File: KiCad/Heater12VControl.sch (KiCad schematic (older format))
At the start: 11 parts, among them J1 12V, J2 Arduino, J3 Heater, J4 Temp sensor, Q1 SI2308, Q2 IRLR3715

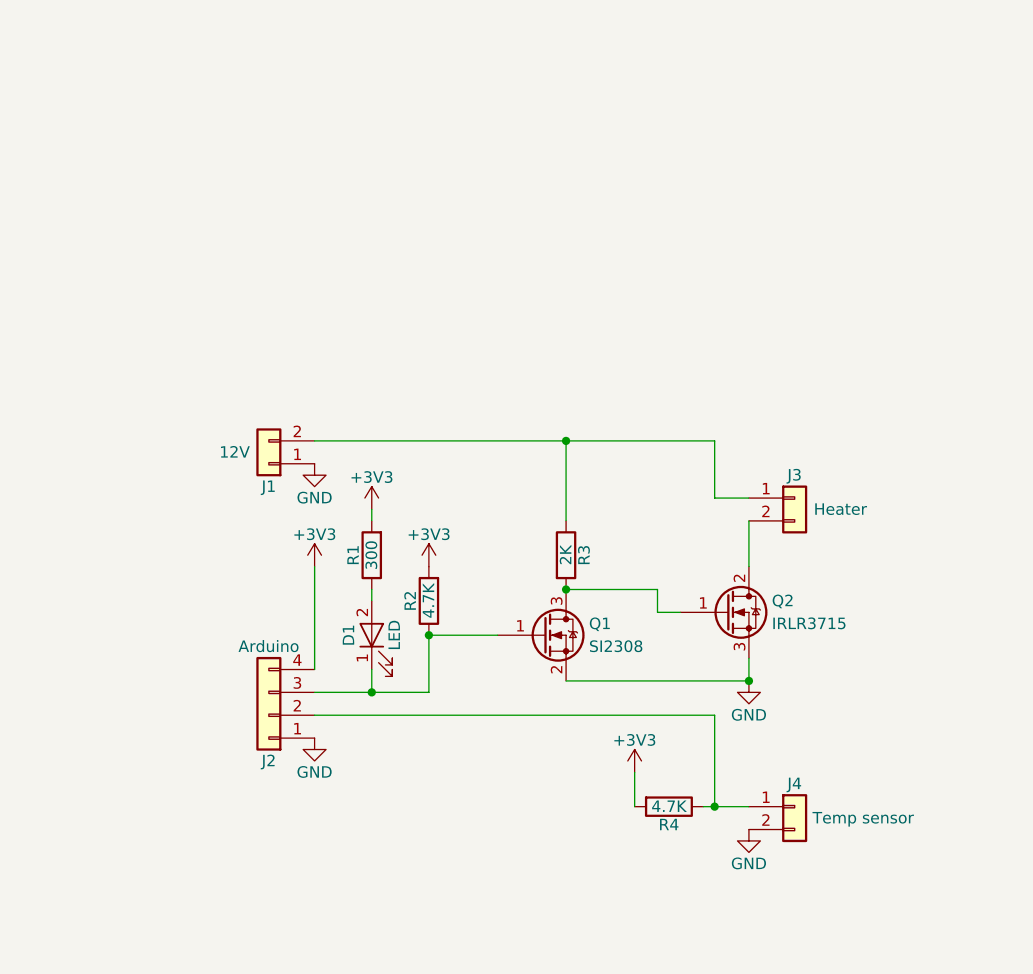
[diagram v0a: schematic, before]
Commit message: New Version with rotary encoder and AIO pcb
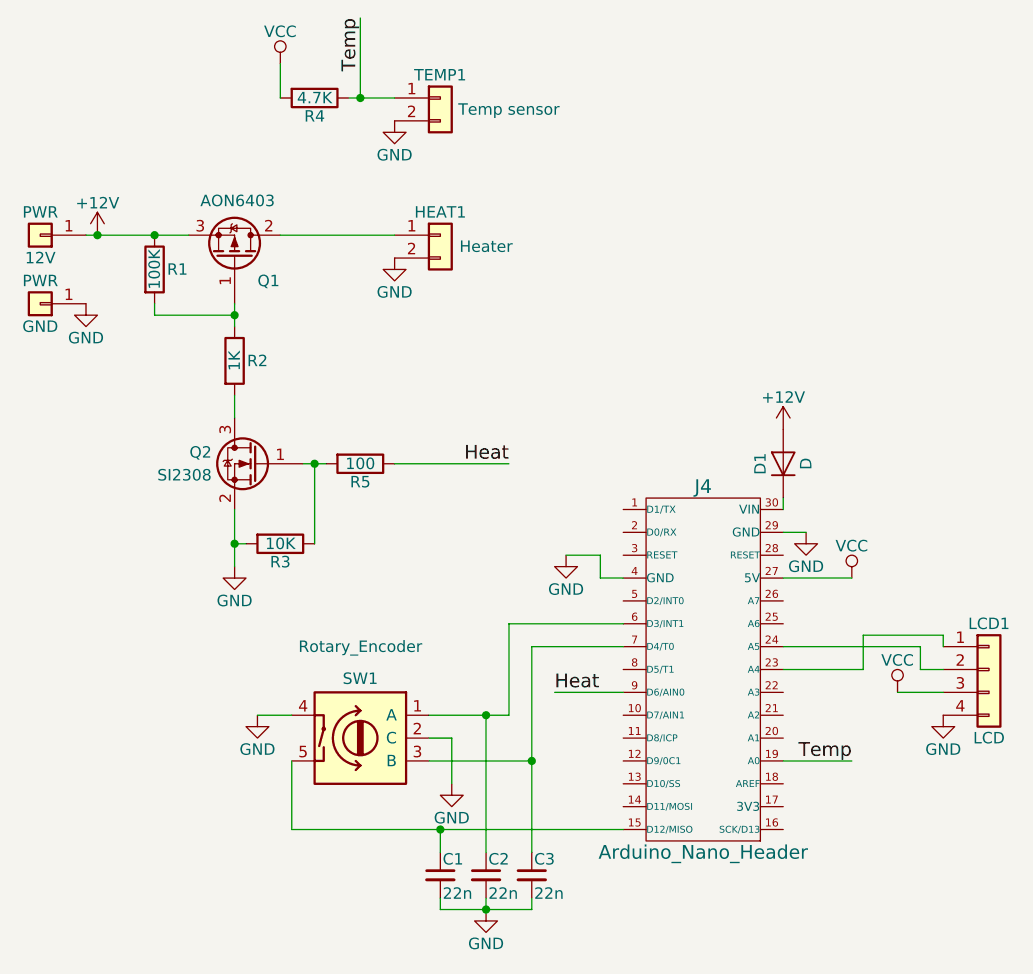
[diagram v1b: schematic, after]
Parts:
- removed D1: LED, LEDs:LED_0805, symbol LED
- removed J1: 12V, Wire_Pads:SolderWirePad_2x_1-2mmDrill, symbol Conn_01x02
- removed J2: Arduino, KiCad_custom:conn_4pin_TH_1.8mm, symbol Conn_01x04
- removed Q2: IRLR3715, TO_SOT_Packages_SMD:TO-252-2_Rectifier, symbol Q_NMOS_GDS
- added 12V, GND: PWR, Pin_Headers:Pin_Header_Angled_1x01_Pitch2.54mm, symbol Conn_01x01
- added C1, C2, C3: 22n, Capacitors_SMD:C_0603, symbol C_Small
- added D1: D, Diodes_SMD:D_SOD-123F, symbol D
- added J4: Arduino_Nano_Header, Modules:Arduino_Nano, symbol Arduino_Nano_Header
- added LCD1: LCD, Pin_Headers:Pin_Header_Straight_1x04_Pitch2.54mm, symbol Conn_01x04
- added Q1: AON6403, KiCadCustomLibs:DFN-8-1EP_6x5mm, symbol Q_PMOS_GDS
- added R5: 100, Resistors_SMD:R_0603, symbol R
- added SW1: Rotary_Encoder, KiCadCustomLibs:SF-ROTARY-ENCODER, symbol Rotary_Encoder_Switch
- HEAT1: renamed from J3; footprint Wire_Pads:SolderWirePad_2x_1-2mmDrill -> Pin_Headers:Pin_Header_Straight_1x02_Pitch2.54mm
- R1: value 300 -> 100K
- R2: value 4.7K -> 1K
- R3: value 2K -> 10K
- TEMP1: renamed from J4; footprint Wire_Pads:SolderWirePad_2x_1-2mmDrill -> Pin_Headers:Pin_Header_Straight_1x02_Pitch2.54mm
- renumbered Q1 to Q2
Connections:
- net GND: now also HEAT1.2 (Pin_2), R3.2, C1.2, C2.2, C3.2, GND.1 (Pin_1), J4.29 (GND), J4.4 (GND), LCD1.4 (Pin_4), SW1.2 (C), SW1.4
- net at Q2.3 (D): now also R2.2; no longer R3.2
- net at HEAT1.1 (Pin_1): now also Q1.2 (D); no longer R3.1
- net at Q2.1 (G): now also R3.1, R5.2; no longer R2.1
- net Temp: now reaches R4.1, TEMP1.1 (Pin_1)
- net Temp: now also J4.19 (A0)
- net +12V: now reaches R1.1
- net +12V: now also 12V.1 (Pin_1), D1.2 (A), Q1.3 (S)
- removed net +3V3: R1.2, R2.2, R4.2
- new net: Q1.1 (G), R1.2, R2.1
- new net: C1.1, J4.15 (D12/MISO), SW1.5
- new net: J4.23 (A4), LCD1.1 (Pin_1)
- new net: J4.24 (A5), LCD1.2 (Pin_2)
- new net: D1.1 (K), J4.30 (VIN)
- new net: C2.1, J4.6 (D3/INT1), SW1.1 (A)
- new net: C3.1, J4.7 (D4/T0), SW1.3 (B)
- new net Heat: J4.9 (D6/AIN0), R5.1
- new net VCC: J4.27 (5V), LCD1.3 (Pin_3), R4.2
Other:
- moved on the sheet: HEAT1, Q2, R4, TEMP1
